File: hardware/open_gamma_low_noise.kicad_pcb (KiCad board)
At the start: 4 copper layers, 50.8 x 77.2 mm, 62 parts, among them J1 1909763-1, J2 1909763-1, Q1 2N7002,215, U1 TLV3201AIDBVR, U2 LM4040AIM3-3.0+T, U3 Pico, U4 OPA357AIDBVTG4, U5 MAX5026EUT+T, U6 LM4040AIM3-3.0+T, U7 OPA357AIDBVTG4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

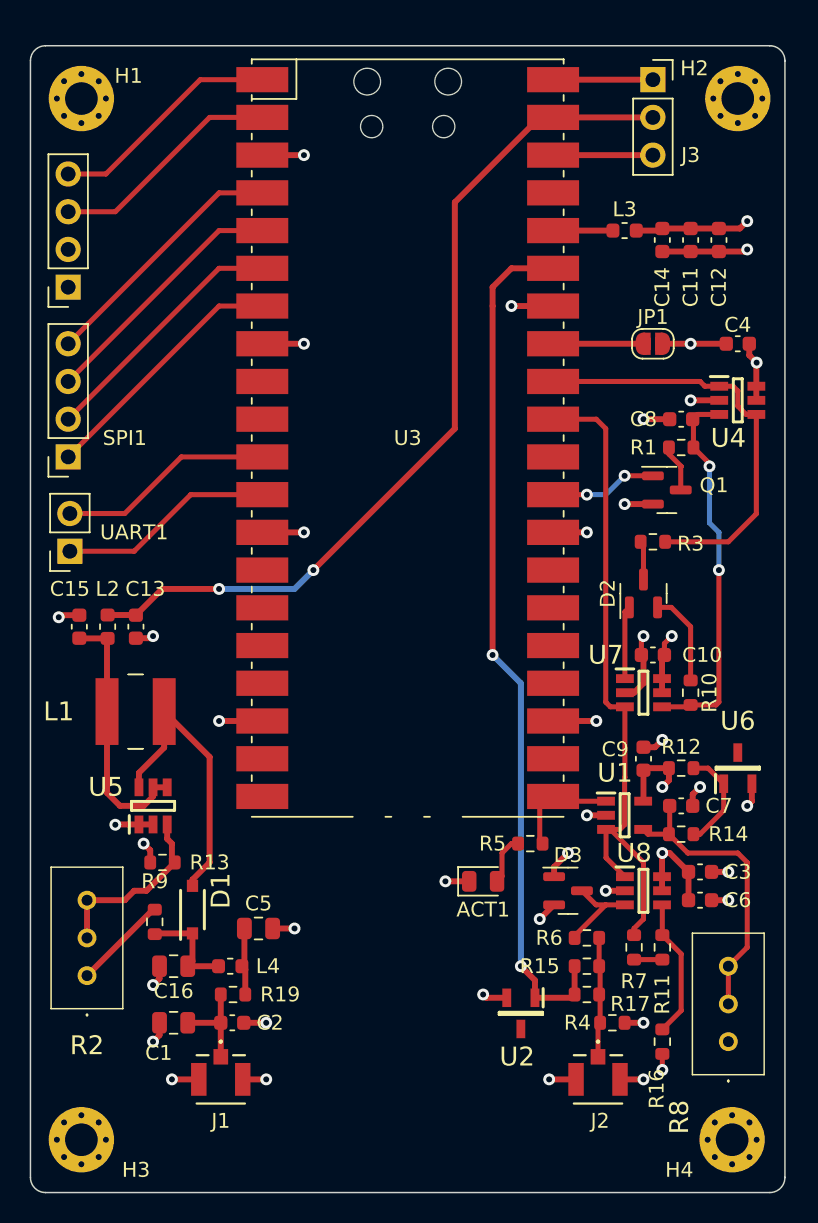
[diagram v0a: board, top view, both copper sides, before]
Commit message: Updated 3D models
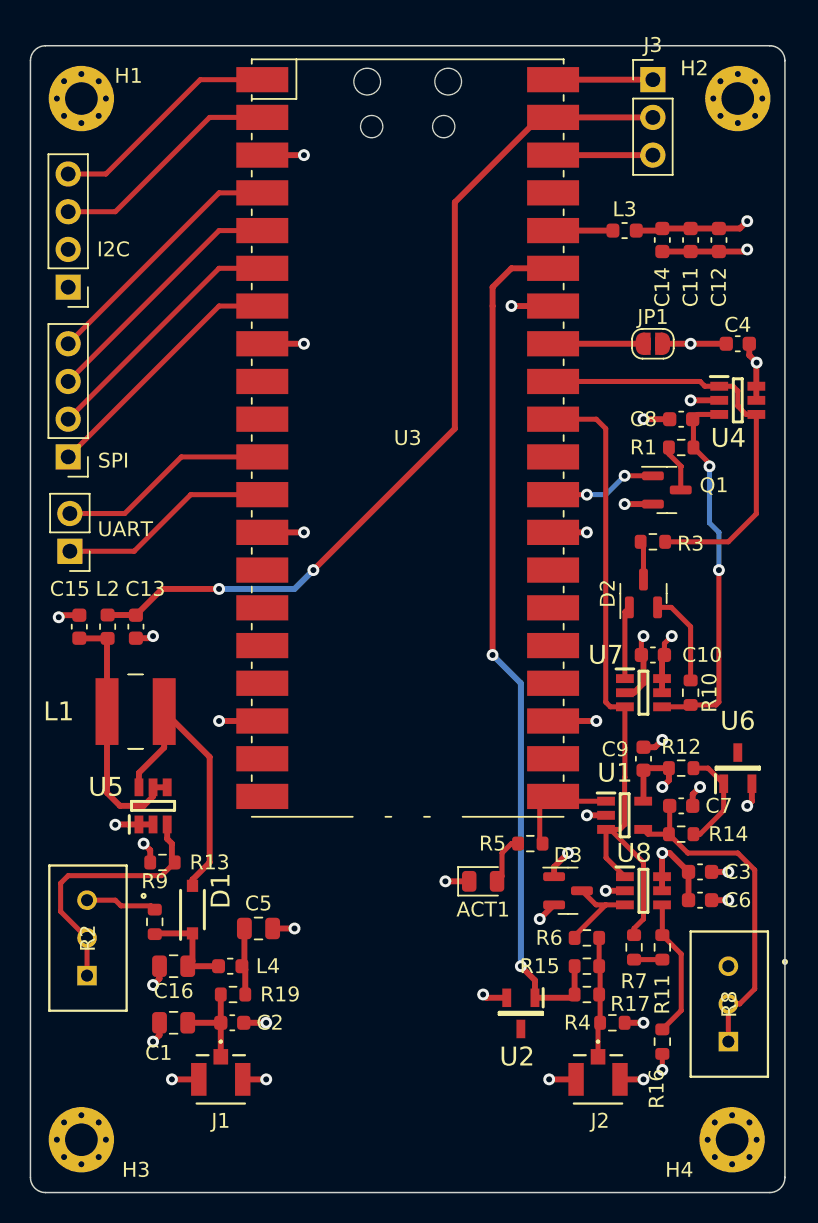
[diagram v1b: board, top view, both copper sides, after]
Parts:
- I2C: renamed from I2C1; footprint Connector_PinSocket_2.54mm:PinSocket_1x04_P2.54mm_Vertical -> Connector_PinHeader_2.54mm:PinHeader_1x04_P2.54mm_Vertical
- J3: footprint Connector_PinSocket_2.54mm:PinSocket_1x03_P2.54mm_Vertical -> Connector_PinHeader_2.54mm:PinHeader_1x03_P2.54mm_Vertical
- R2, R8: footprint 3296W-1-103:3296W1103 -> Trimmer_Res:POT_3296W
- SPI: renamed from SPI1; footprint Connector_PinSocket_2.54mm:PinSocket_1x04_P2.54mm_Vertical -> Connector_PinHeader_2.54mm:PinHeader_1x04_P2.54mm_Vertical
- UART: renamed from UART1; footprint Connector_PinSocket_2.54mm:PinSocket_1x02_P2.54mm_Vertical -> Connector_PinHeader_2.54mm:PinHeader_1x02_P2.54mm_Vertical
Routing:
- net Net-(U5-FB): track 12.3 -> 18.0 mm
- net Net-(U1-IN-): track 19.9 -> 23.3 mm
- net Net-(R2-Pad1): track 6.40 -> 4.94 mm
